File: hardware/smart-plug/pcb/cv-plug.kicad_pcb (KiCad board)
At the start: 2 copper layers, 88.8 x 89.8 mm, 39 parts, among them J1 Plug pins + socket, K1 T90/HF105 16A, Q1 S8050, SW1 Tactile 6mm, U1 ESP32-WROOM-32E (4MB), U2 AMS1117-3.3, U3 BL0937 / HLW8032, U4 PC817

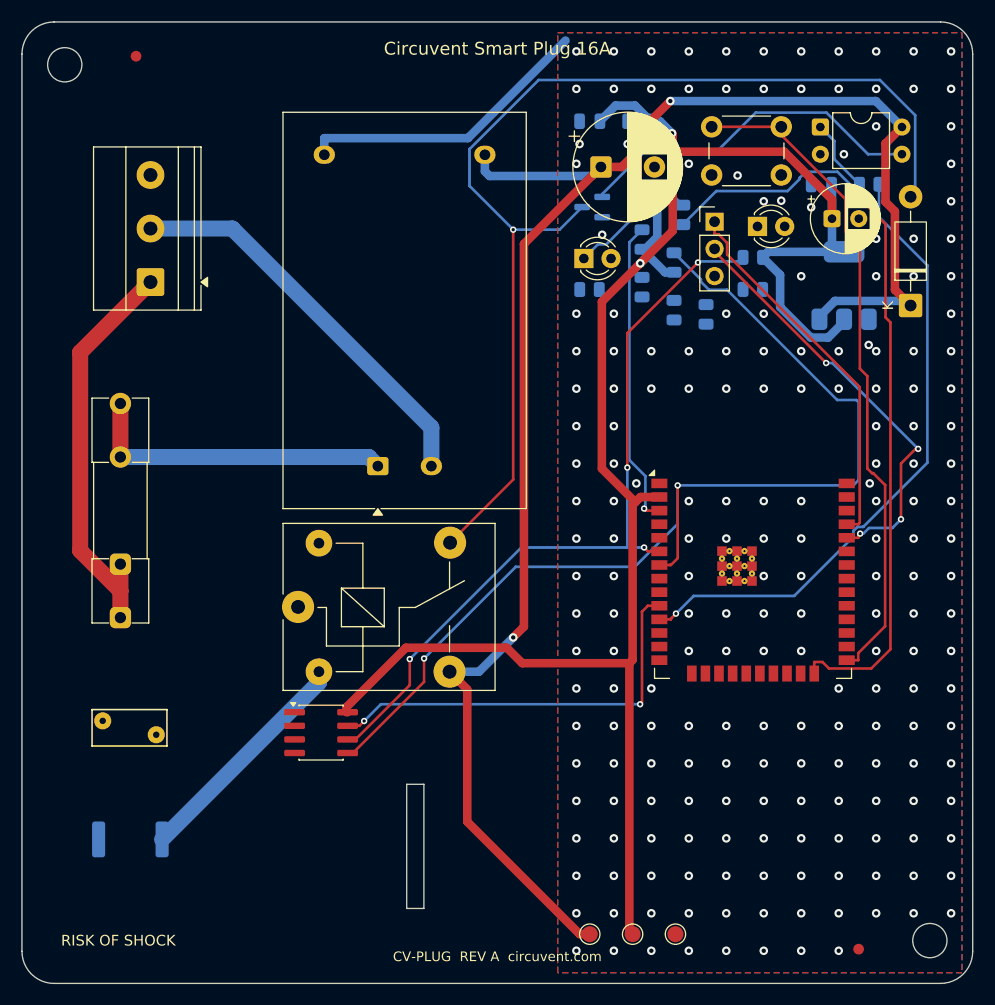
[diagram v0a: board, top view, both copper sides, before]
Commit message: hardware: fix mains isolation barrier gaps, add load-controller PCB
Adds the 13th board (ultra-compact dual-channel load controller: ESP32-C3,
opto+relay channel, MOSFET PWM channel, USB-C, AP2112K LDO, USBLC6 ESD) and
regenerates all 12 existing boards, which were stale with respect to earlier
relay-pinout and LED-polarity fixes.

The substantive change is to the mains isolation barrier. It is a keepout band
the router must not cross, deliberately cut where a component straddles it
because there the isolation is provided by the part's package. Three linked
defects made those cuts unsafe, each only visible once the previous was fixed:

1. The cut removed the barrier across the full band width for the straddling
   part's whole height, while the ISO_BRIDGE area that excuses the gap covered
   only the part itself. The router used the leftover strip beside the part to
   bring +5V within 6.99 mm of AC_N against an 8.0 mm reinforced creepage rule.
2. Straddling parts can overlap in y, so cutting per part put one part's
   keepout on another part's pads. The exempt x-ranges are now unioned per
   strip by a sweep line.
3. The rule only relaxes for items insideArea('ISO_BRIDGE'). With the hole the
   same size as the area, a track could hug the hole's edge without being
   contained in it, so the rule fired anyway and the router had no way to know.
   The hole is now the part's pad bbox + 0.3 mm, strictly inside ISO_BRIDGE at
   the footprint bbox + 0.6 mm.

The tighter hole leaves mains nets less room to reach bridge pads, so some
boards report more unconnected items. That is deliberate: those are documented
hand-routing items, whereas a creepage violation is a safety defect.

Also fixed in the generator:
- _pad_shape() derived a pad's layers from PAD::GetLayer(), which returns F.Cu
  even for pads on B.Cu. Every back-side pad became a phantom obstacle on the
  front, blocking legal paths there while hiding the real one behind. Only
  IsOnLayer() is truthful.
- Castella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
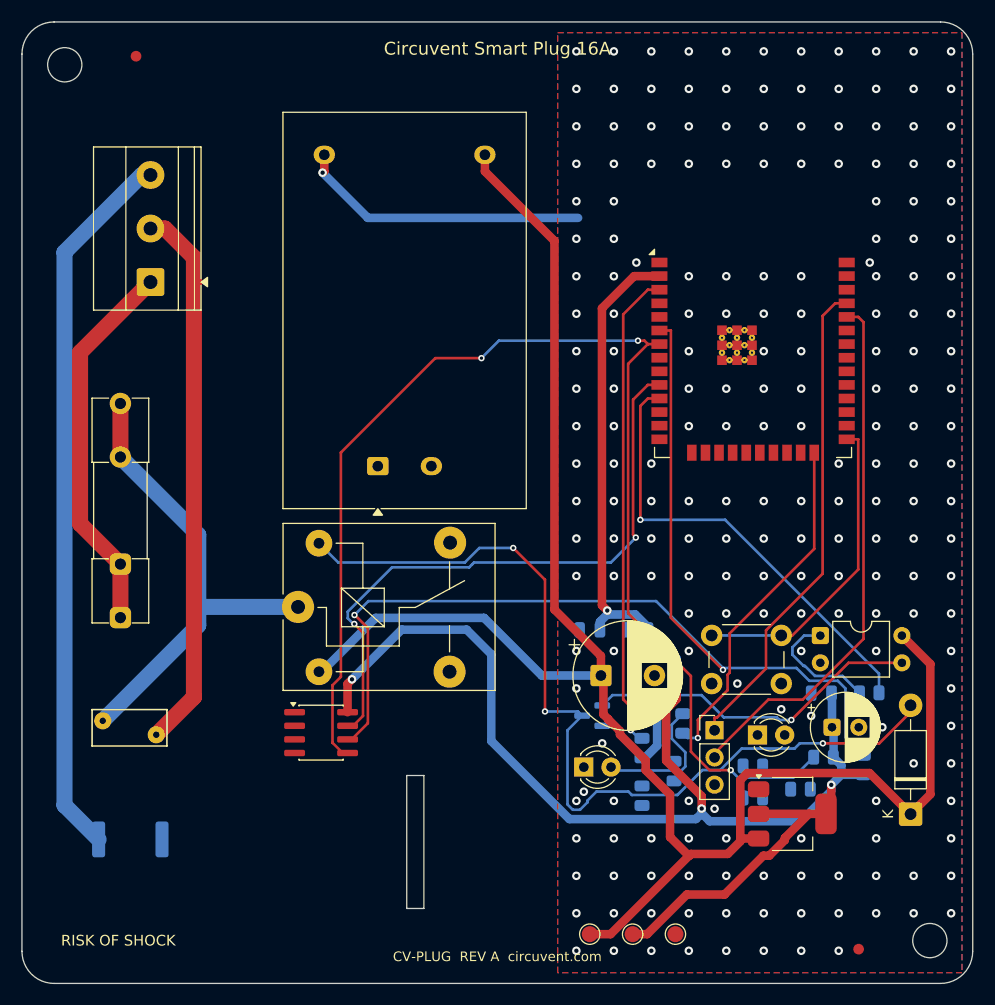
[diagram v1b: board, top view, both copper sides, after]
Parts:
- U2: moved to F.Cu
- moved U2 49.6 mm to (171.9, 154.0), turned to 0 degrees
- moved R5 48.5 mm to (178.6, 149.4), turned to 90 degrees
- moved R4 48.3 mm to (174.9, 148.7), turned to 180 degrees
- moved R8 47.5 mm to (157.9, 152.3), turned to 90 degrees
- moved D1 47.5 mm to (183.0, 154.0)
- moved R2 47.5 mm to (161.7, 145.5)
- moved C2 47.5 mm to (175.7, 145.9)
- moved C3 47.5 mm to (153.0, 136.8)
- moved C4 47.5 mm to (157.5, 136.8)
- moved C5 47.5 mm to (174.7, 142.7)
- moved C6 47.5 mm to (158.0, 144.1)
- moved JP 47.5 mm to (164.7, 146.2)
- moved LED0 47.5 mm to (168.7, 146.6)
- moved LED1 47.5 mm to (152.5, 149.6)
- moved R1 47.5 mm to (179.1, 142.7)
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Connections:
- K1 pad 2: RELAY_PIN_SW -> +5V
- K1 pad 3: +5V -> RELAY_PIN_SW
- K1 pad 4: RELAY_PIN_COIL -> N$K1.4
- K1 pad 5: N$K1.5 -> RELAY_PIN_COIL
- LED1 pad 1: LED_PIN_A -> GND
- LED1 pad 2: GND -> LED_PIN_A
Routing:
- net AC_LOAD: track 0.00 -> 67.2 mm
- net LED_PIN: track 72.5 -> 32.7 mm
- net BTN_PIN: track 62.8 -> 29.5 mm
- net MTR_CF1: track 71.9 -> 104.8 mm, vias 4 -> 2
- net RELAY_PIN_SW: track 21.7 -> 0.00 mm
- net MTR_SEL: track 38.7 -> 58.0 mm
- net MTR_CF: track 100.9 -> 118.0 mm, vias 2 -> 3
- net RELAY_PIN: track 59.3 -> 42.7 mm
- net AC_L_FUSED: track 29.4 -> 45.7 mm
- net RELAY_PIN_COIL: track 101.7 -> 85.5 mm, vias 1 -> 3
- net EN: track 28.7 -> 44.8 mm
- net AC_N: track 37.5 -> 51.2 mm
- net UART_TX: track 35.2 -> 45.7 mm
- net UART_RX: track 40.2 -> 50.1 mm, vias 4 -> 0
- net +5V: track 158.5 -> 165.4 mm, vias 2 -> 0
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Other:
- outline, holes or cut-outs redrawn

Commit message: Release 1.10.0, and stop shipping permissions the app never uses
Cut 1.10.0 (versionCode 12) and built it: AAB 38 MB, APK 83 MB, signed with the
upload key, JS bundle embedded.

Checking the generated manifest before writing the Play listing turned up
permissions no one had asked for. Every one of them is printed on the store page
for users to read before they install:

  RECORD_AUDIO          expo-camera asks for the microphone so video can be
                        recorded with sound. This app only ever puts the camera
                        in barcode mode to read a QR label, and expo-speech is
                        output-only - it speaks, it does not listen. Left in,
                        Play lists "Microphone" against a home-control app,
                        which is alarming, unexplainable and untrue.
  SYSTEM_ALERT_WINDOW   React Native's development overlay, useless in a release
                        build and shown to users as "Display over other apps".
  READ/WRITE_EXTERNAL_STORAGE
                        Legacy storage access nothing here touches.

Stripped via android.blockedPermissions. That emits tools:node="remove", which
is a merge instruction rather than a guarantee, so it was checked against the
finished artifact with aapt2 rather than the source manifest - all four are
absent from the APK.

NEARBY_WIFI_DEVICES now carries neverForLocation. Android otherwise treats it as
location-capable, because knowing which networks are in range is enough to place
someone, and Play's data safety review treats it the same way. The app uses it
only to join a new device's setup hotspot. That flag is a promise, so the plugin
says plainly that it has to come off if scan results are ever used positionally.

What is left is defensible: location for Wi-Fi onboarding (Android requires it),
camera for the QR label, nearby-devices flagged as non-positional.

Added mobile/store/listing with the text Play asks for - title, short and full
descriptions, and what'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
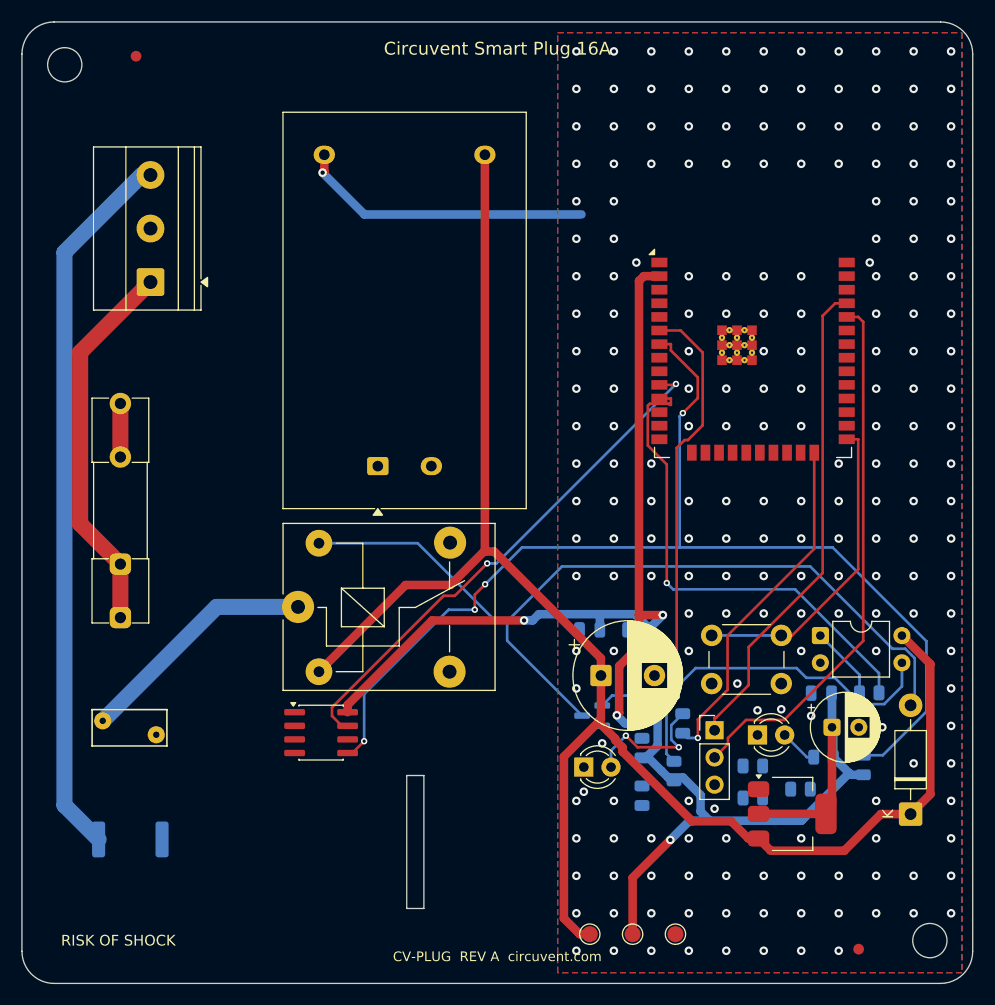
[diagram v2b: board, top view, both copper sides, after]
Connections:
- LED0 pad 1: N$LED0.1 -> GND
- LED0 pad 2: N$LED0.2 -> LED0_A
- R4 pad 2: MTR_CF -> LED0_A
- R5 pad 2: MTR_CF1 -> MTR_CF
- R6 pad 1: N$R6.1 -> +3V3
- R6 pad 2: N$R6.2 -> MTR_CF1
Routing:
- net MTR_CF1: track 104.8 -> 45.0 mm, vias 2 -> 1
- net AC_N: track 51.2 -> 0.00 mm
- net EN: track 44.8 -> 0.00 mm, vias 1 -> 0
- net +3V3: track 174.5 -> 155.9 mm, vias 6 -> 4
- net AC_L_FUSED: track 45.7 -> 27.7 mm
- net MTR_CF: track 118.0 -> 105.0 mm, vias 3 -> 4
- net +5V: track 165.4 -> 155.3 mm
- net MTR_SEL: track 58.0 -> 48.9 mm
- net RELAY_PIN_COIL: track 85.5 -> 80.6 mm, vias 3 -> 0
- net RELAY_PIN_OPT: track 11.5 -> 6.86 mm
- net RELAY_PIN: track 42.7 -> 46.4 mm
- net LED0_A: track 0.00 -> 3.57 mm
- net RELAY_PIN_DRV: track 31.6 -> 34.1 mm, vias 1 -> 0
- net GND: track 28.0 -> 27.6 mm, vias 212 -> 213
- net LED_PIN_A: track 13.1 -> 12.8 mm, vias 0 -> 2
